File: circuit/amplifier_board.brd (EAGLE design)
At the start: 60 x 30 mm, 17 parts

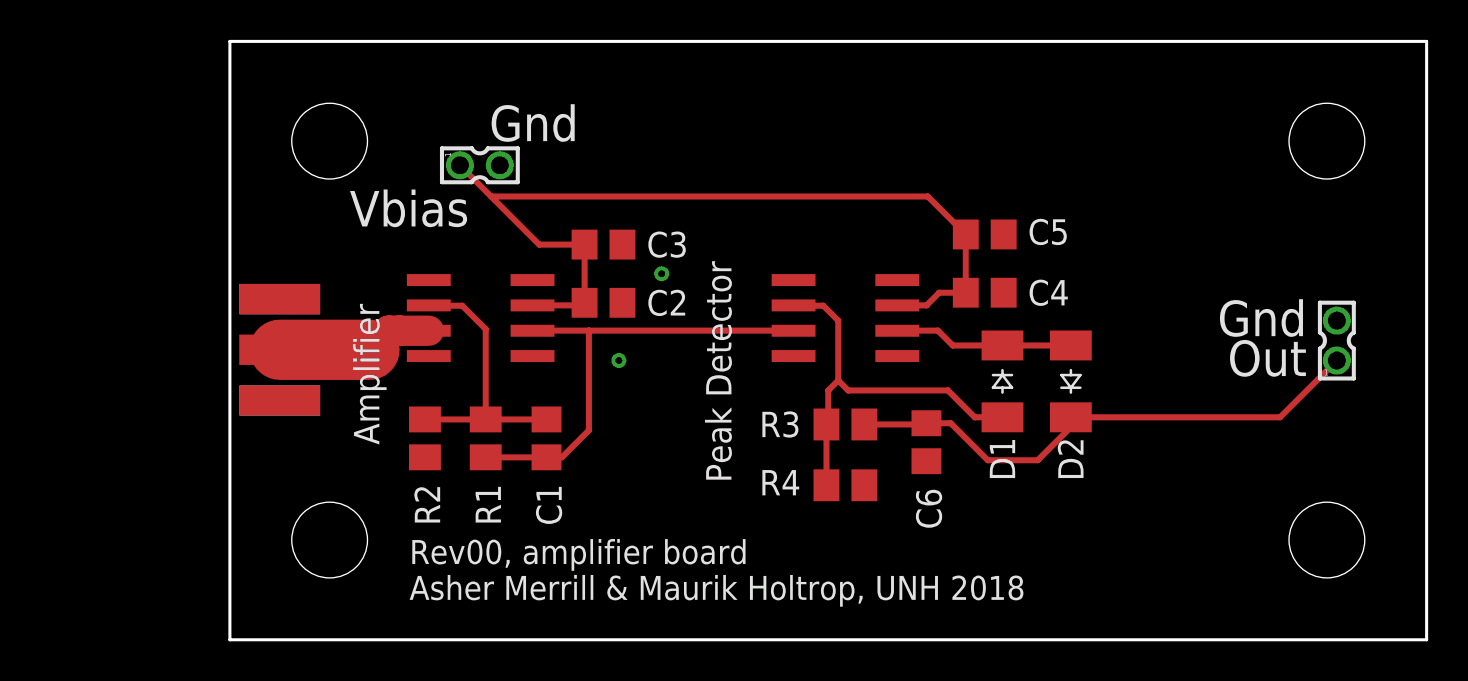
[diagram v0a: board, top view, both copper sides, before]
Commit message: boards: Changed packages of cap and resistors to be 0603, as we will have available.  Also changed mount points to be grounded, and made vias solderable.
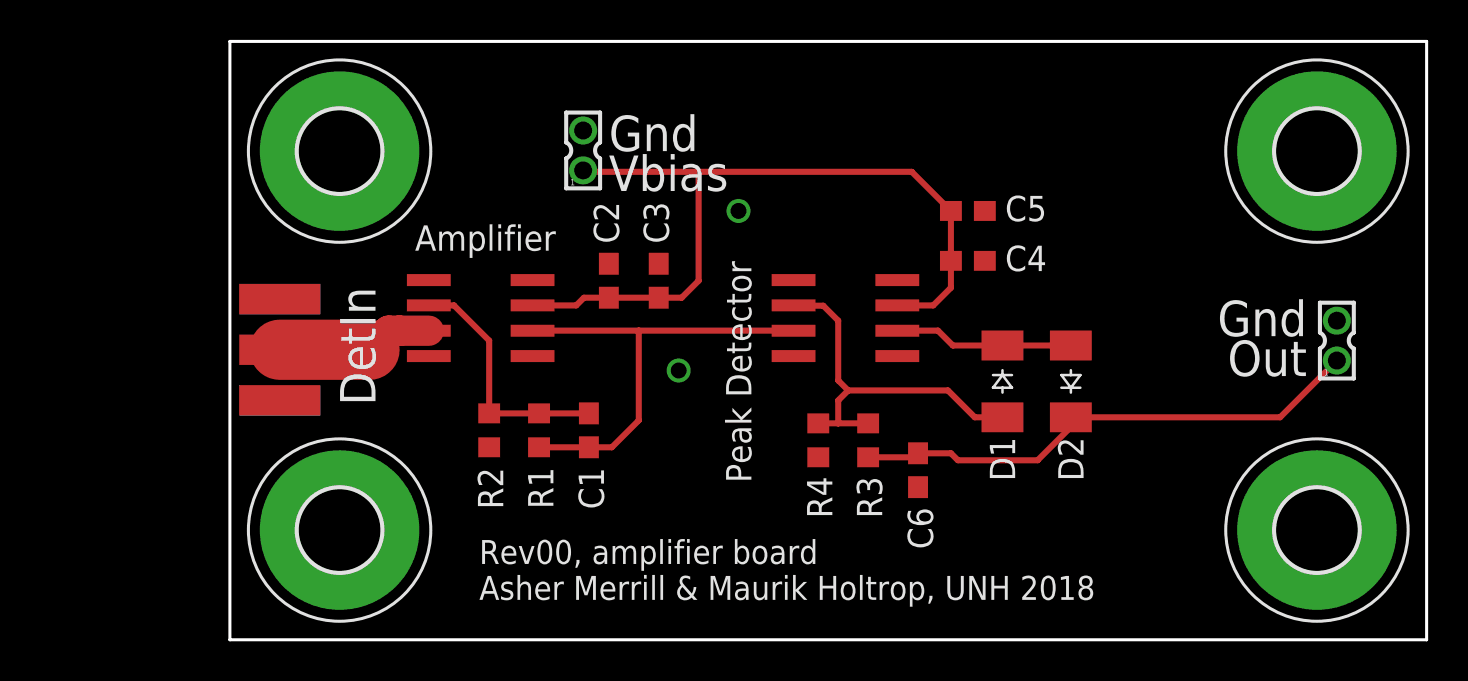
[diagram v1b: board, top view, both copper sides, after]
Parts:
- added H1, H2, H3, H4: MOUNT-PAD-ROUND4.1, holes:4,1-PAD
- C1, C2, C3, C4, C5, C6: device rcl:C0805 -> rcl:C0603
- R1, R2, R3, R4: device rcl:M0805 -> rcl:R0603
- moved SUP 5.23 mm to (17.7, 24.5), turned to 0 degrees
- moved C3 3.31 mm to (21.5, 18.0), turned to 90 degrees
- moved R2 3.25 mm to (13.0, 10.5), turned to 90 degrees
- moved R1 2.70 mm to (15.5, 10.5)
- moved R4 2.63 mm to (29.5, 10.0), turned to 90 degrees
- moved C1 2.16 mm to (18.0, 10.5)
- moved C4 1.81 mm to (37.0, 19.0)
- moved C6 1.47 mm to (34.5, 8.50)
- moved C5 1.45 mm to (37.0, 21.5)
- moved R3 1.39 mm to (32.0, 10.0), turned to 270 degrees
- moved C2 1.14 mm to (19.0, 18.0), turned to 90 degrees
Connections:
- net GND: now also H1.B4,1, H2.B4,1, H3.B4,1, H4.B4,1, R2.1, R4.1; no longer R2.2, R4.2
- net IN-_1: now also R2.2; no longer R2.1
- net IN-_2: now also R4.2; no longer R4.1
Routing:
- net VCC: track 44.7 -> 40.5 mm
- net IN-_1: track 14.0 -> 12.4 mm
- net IN-_2: track 20.9 -> 19.8 mm
- net DIG_READOUT: track 26.8 -> 26.1 mm
- net AMP: track 23.8 -> 23.2 mm
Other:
- board text added: "DetIn"

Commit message: Modified board. Tried to add Spice model.
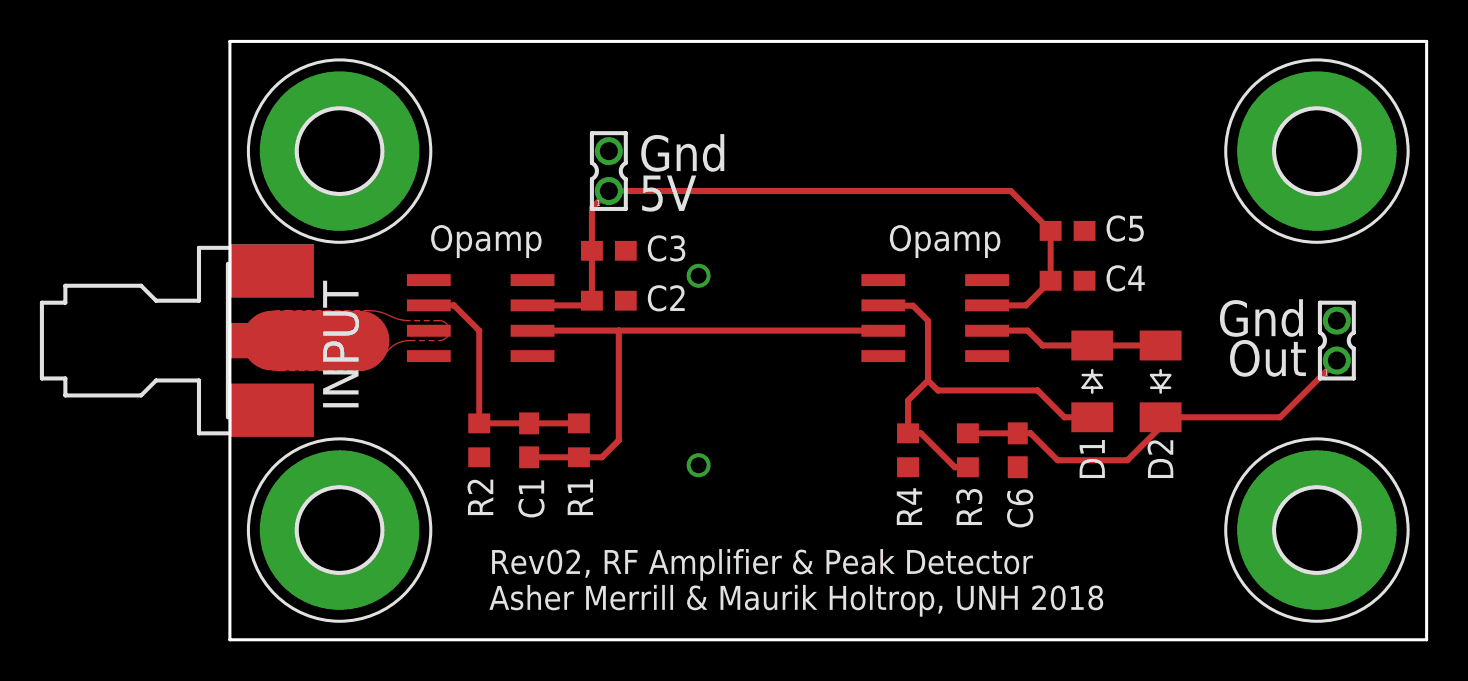
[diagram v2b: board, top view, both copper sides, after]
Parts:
- removed IN: SMA_EDGE, SparkFun-Retired:SMA-EDGE
- added INPUT: Input, 000phys605parts:SMA-EDGE
- MAX4104_1: value Amplifier -> Opamp
- MAX4104_2: value Peak Detector -> Opamp
- moved H2 52.6 mm to (5.50, 24.5)
- moved H4 52.6 mm to (54.5, 24.5), turned to 90 degrees
- moved H1 19.0 mm to (5.50, 5.50)
- moved H3 19.0 mm to (54.5, 5.50)
- moved C4 5.10 mm to (42.0, 18.0)
- moved C5 5.10 mm to (42.0, 20.5)
- moved C6 5.10 mm to (39.5, 9.50)
- moved R3 5.02 mm to (37.0, 9.50), turned to 90 degrees
- moved R4 4.53 mm to (34.0, 9.50)
- moved D1 4.50 mm to (43.2, 13.0)
- moved D2 4.50 mm to (46.7, 13.0)
- moved MAX4104_2 4.50 mm to (35.4, 16.1)
- moved C1 3.04 mm to (15.0, 10.0)
- moved C3 2.92 mm to (19.0, 19.5), turned to 0 degrees
- moved R1 2.06 mm to (17.5, 10.0)
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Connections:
- net GND: now also INPUT.G@1, INPUT.G@2, INPUT.G@3, INPUT.G@4; no longer IN.GND@0, IN.GND@1, IN.GND@2, IN.GND@3
- net IN: now also INPUT.G@0; no longer IN.SIG
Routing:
- net AMP: track 23.2 -> 27.9 mm
- net DIG_READOUT: track 26.1 -> 21.4 mm
- net IN: track 7.87 -> 4.38 mm
- net IN-_2: track 19.8 -> 22.2 mm
- net VCC: track 40.5 -> 38.1 mm
- added copper zone on layer 1, net IN
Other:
- board text added: "5V"
- board text added: "Rev02, RF Amplifier & Peak Detector Asher Merrill & Maurik Holtrop, UNH 2018"
- board text removed: "DetIn"
- board text removed: "Rev00, amplifier board Asher Merrill & Maurik Holtrop, UNH 2018"
- board text removed: "Vbias"

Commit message: boards: Added VEE line to header.  Corrected header to be 0.100", (what we have in stock,) not 2mm header.
Also added filtering caps (backwards, sort of,) to stabilize the VEE line.
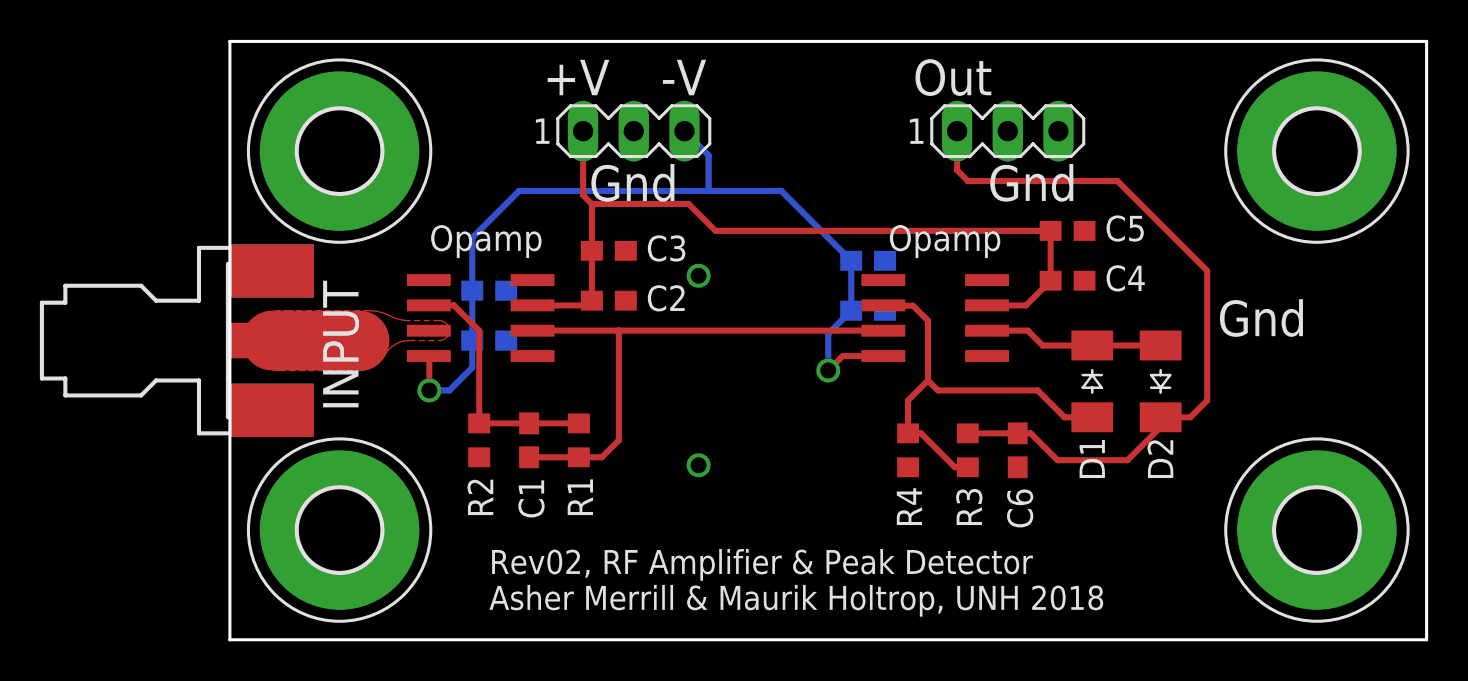
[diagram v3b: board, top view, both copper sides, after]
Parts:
- removed SUP, SUP1: 332-02, con-garry:332-02
- added C10, C8: 10uF, rcl:C0603
- added C7, C9: 0.1uF, rcl:C0603
- added SV1, SV2: (no value), con-lstb:MA03-1
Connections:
- new net VEE: C10.2, C7.2, C8.2, C9.2, MAX4104_1.4, MAX4104_2.4, SV1.3
- net DIG_READOUT: now also SV2.1; no longer SUP1.1
- net GND: now also C10.1, C7.1, C8.1, C9.1, SV1.2, SV2.2, SV2.3; no longer MAX4104_1.4, MAX4104_2.4, SUP.2, SUP1.2
- net VCC: now also SV1.1; no longer SUP.1
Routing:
- net VEE: track 0.00 -> 44.8 mm, vias 0 -> 2
- net DIG_READOUT: track 21.4 -> 37.2 mm
- net VCC: track 38.1 -> 41.5 mm
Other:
- board text added: "+V"
- board text added: "-V"
- board text removed: "5V"
